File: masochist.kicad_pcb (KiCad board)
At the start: 2 copper layers, 202.4 x 100.8 mm, 88 parts, among them J1 USB_C_Receptacle_USB2.0, J2 AVR-ISP-6, SW1 RESET, SW2 SW_Push, U1 ATmega328P-PU, Y1 Crystal

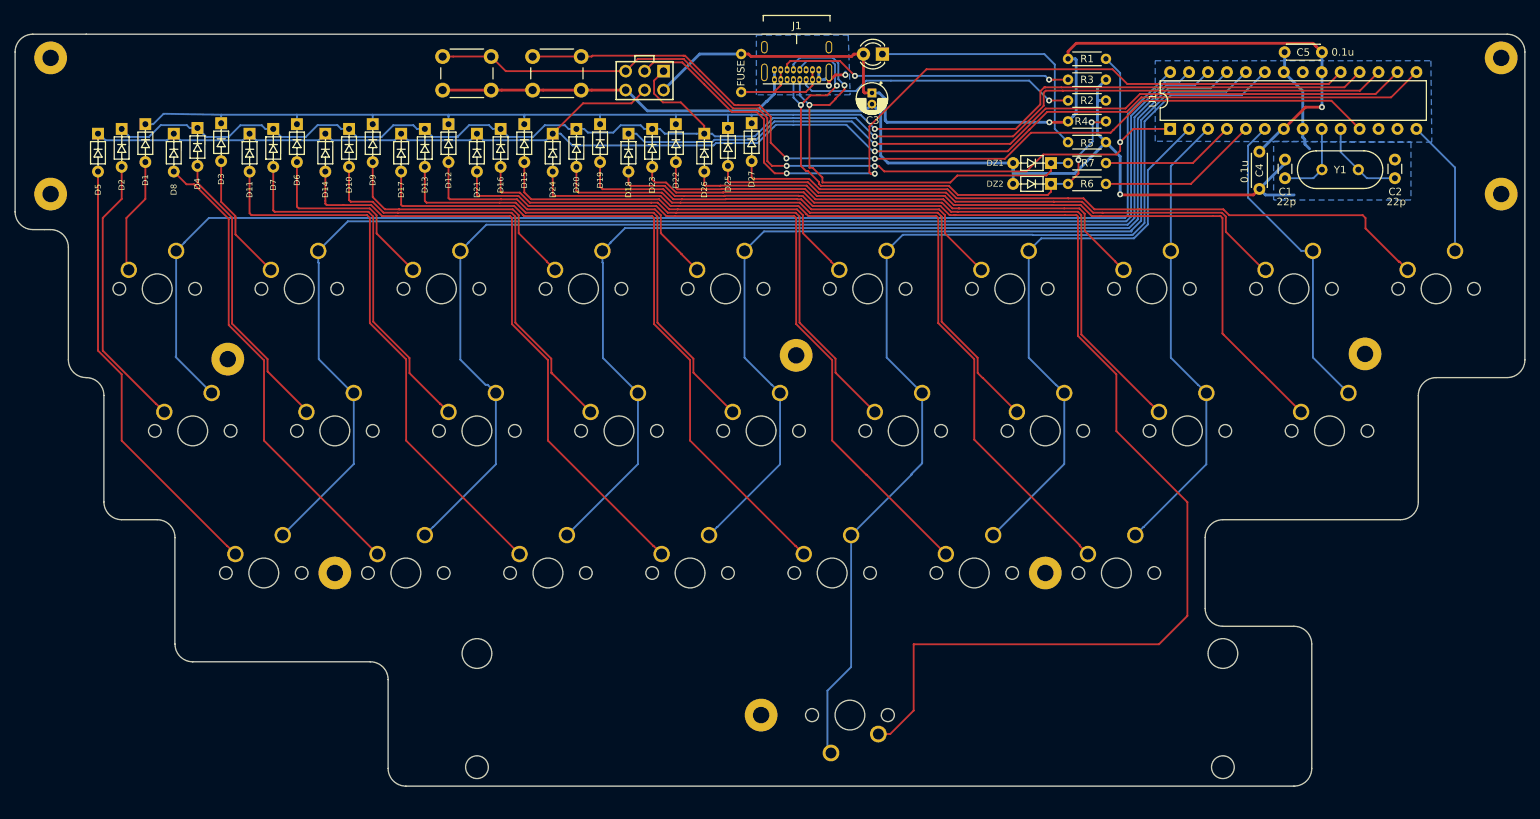
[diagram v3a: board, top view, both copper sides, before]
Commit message: added more mounting holes i love mounting holes
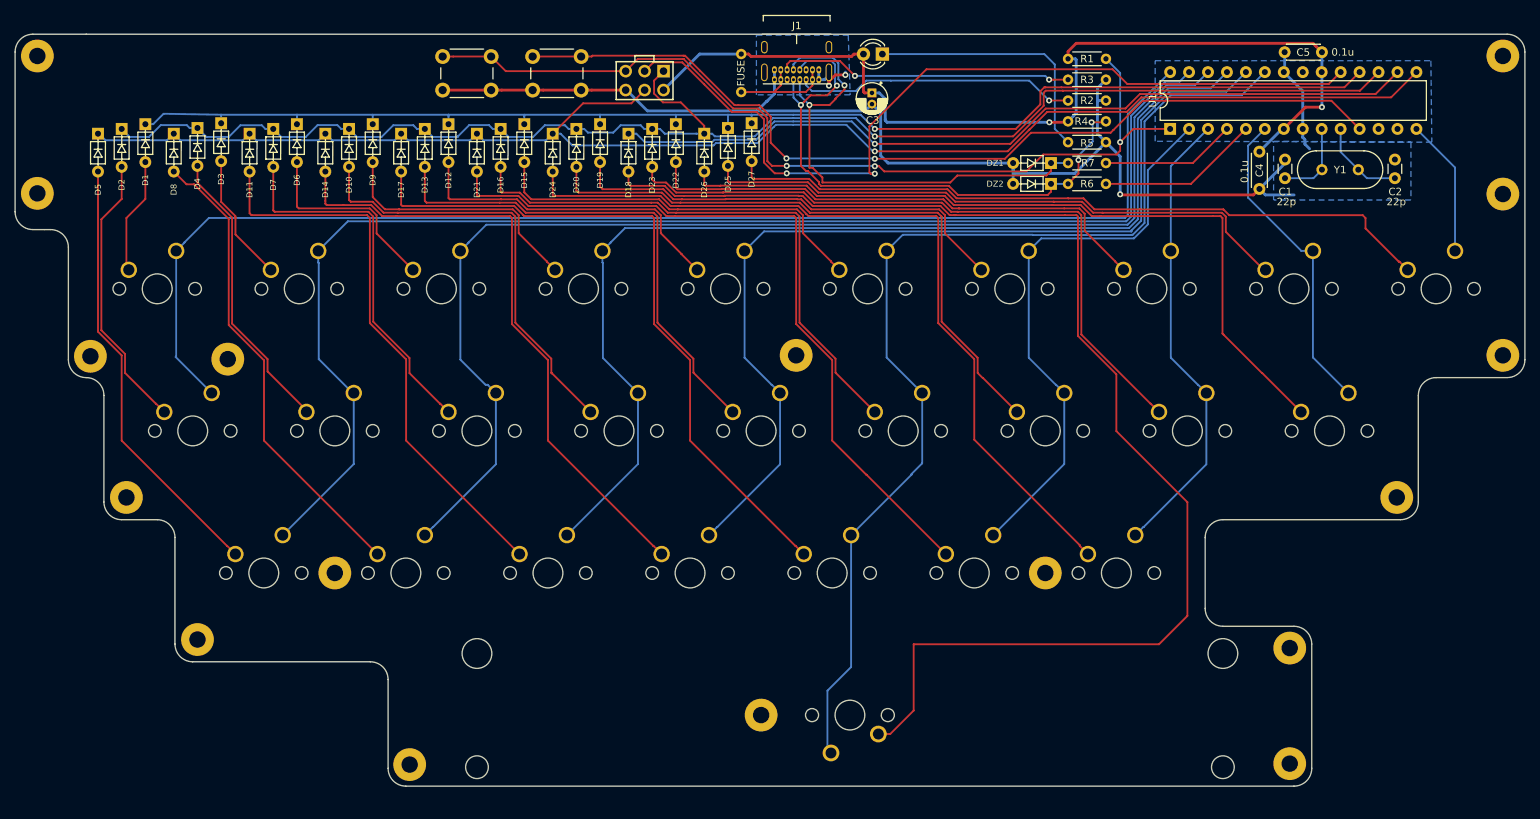
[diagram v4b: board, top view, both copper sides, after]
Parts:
- removed the REF** at (63.5, 34.9)
- removed the REF** at (258.0, 53.2)
- added REF**: MountingHole_2.2mm_M2_Pad, cftkb:MountingHole_2.2mm_M2_Pad, F.Cu at (68.8, 74.9)
- added REF**: MountingHole_2.2mm_M2_Pad, cftkb:MountingHole_2.2mm_M2_Pad, F.Cu at (61.7, 34.7)
- added REF**: MountingHole_2.2mm_M2_Pad, cftkb:MountingHole_2.2mm_M2_Pad, F.Cu at (258.2, 53.2)
- added REF**: MountingHole_2.2mm_M2_Pad, cftkb:MountingHole_2.2mm_M2_Pad, F.Cu at (73.7, 93.9)
- added REF**: MountingHole_2.2mm_M2_Pad, cftkb:MountingHole_2.2mm_M2_Pad, F.Cu at (83.2, 112.9)
- added REF**: MountingHole_2.2mm_M2_Pad, cftkb:MountingHole_2.2mm_M2_Pad, F.Cu at (111.6, 129.7)
- added REF**: MountingHole_2.2mm_M2_Pad, cftkb:MountingHole_2.2mm_M2_Pad, F.Cu at (229.6, 129.5)
- added REF**: MountingHole_2.2mm_M2_Pad, cftkb:MountingHole_2.2mm_M2_Pad, F.Cu at (229.6, 114.0)
- added REF**: MountingHole_2.2mm_M2_Pad, cftkb:MountingHole_2.2mm_M2_Pad, F.Cu at (244.0, 93.9)
- moved REF** 18.5 mm to (258.2, 74.8)
- moved G*** 4.83 mm to (163.4, 45.8)
- moved REF** 1.78 mm to (61.7, 53.1)
- moved REF** 0.34 mm to (258.2, 34.7)
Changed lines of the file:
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@@
     (thickness 1.6)
     (drawings 38)
-    (tracks 968)
+    (tracks 970)
     (zones 0)
-    (modules 88)
+    (modules 95)
     (nets 62)
   )
@@
     (add_net GND)
   )
+  (module cftkb:MountingHole_2.2mm_M2_Pad (layer F.Cu)
+    (at 68.834 74.93)
+    (descr "Mounting Hole 2.2mm, M2")
+    (tags "mounting hole 2.2mm m2")
+    (attr virtual)
+    (fp_text reference REF** (at 0 -3.2) (layer Cmts.User)
+      (effects (font (size 1 1) (thickness 0.15)))
+    )
+    (fp_text value MountingHole_2.2mm_M2_Pad (at 0 3.2) (layer F.Fab)
+      (effects (font (size 1 1) (thickness 0.15)))
+    )
+    (fp_circle (center 0 0) (end 2.45 0) (layer F.CrtYd) (width 0.05))
+    (fp_circle (center 0 0) (end 2.2 0) (layer Cmts.User) (width 0.15))
+    (fp_text user %R (at 0.3 0) (layer F.Fab)
+      (effects (font (size 1 1) (thickness 0.15)))
+    )
+    (pad 1 thru_hole circle (at 0 0) (size 4.4 4.4) (drill 2.2) (layers *.Cu *.Mask))
+  )
+  (module cftkb:MountingHole_2.2mm_M2_Pad (layer F.Cu)
+    (at 73.66 93.853)
+    (descr "Mounting Hole 2.2mm, M2")
+    (tags "mounting hole 2.2mm m2")
+    (attr virtual)
+    (fp_text reference REF** (at 0 -3.2) (layer Cmts.User)
+      (effects (font (size 1 1) (thickness 0.15)))
+    )
+    (fp_text value MountingHole_2.2mm_M2_Pad (at 0 3.2) (layer F.Fab)
+      (effects (font (size 1 1) (thickness 0.15)))
+    )
+    (fp_circle (center 0 0) (end 2.45 0) (layer F.CrtYd) (width 0.05))
+    (fp_circle (center 0 0) (end 2.2 0) (layer Cmts.User) (width 0.15))
+    (fp_text user %R (at 0.3 0) (layer F.Fab)
+      (effects (font (size 1 1) (thickness 0.15)))
+    )
+    (pad 1 thru_hole circle (at 0 0) (size 4.4 4.4) (drill 2.2) (layers *.Cu *.Mask))
+  )
+  (module cftkb:MountingHole_2.2mm_M2_Pad (layer F.Cu)
+    (at 83.185 112.903)
+    (descr "Mounting Hole 2.2mm, M2")
+    (tags "mounting hole 2.2mm m2")
+    (attr virtual)
+    (fp_text reference REF** (at 0 -3.2) (layer Cmts.User)
+      (effects (font (size 1 1) (thickness 0.15)))
+    )
+    (fp_text value MountingHole_2.2mm_M2_Pad (at 0 3.2) (layer F.Fab)
+      (effects (font (size 1 1) (thickness 0.15)))
+    )
+    (fp_circle (center 0 0) (end 2.45 0) (layer F.CrtYd) (width 0.05))
+    (fp_circle (center 0 0) (end 2.2 0) (layer Cmts.User) (width 0.15))
+    (fp_text user %R (at 0.3 0) (layer F.Fab)
+      (effects (font (size 1 1) (thickness 0.15)))
+    )
+    (pad 1 thru_hole circle (at 0 0) (size 4.4 4.4) (drill 2.2) (layers *.Cu *.Mask))
+  )
+  (module cftkb:MountingHole_2.2mm_M2_Pad (layer F.Cu)
+    (at 111.633 129.667)
+    (descr "Mounting Hole 2.2mm, M2")
+    (tags "mounting hole 2.2mm m2")
+    (attr virtual)
+    (fp_text reference REF** (at 0 -3.2) (layer Cmts.User)
+      (effects (font (size 1 1) (thickness 0.15)))
+    )
+    (fp_text value MountingHole_2.2mm_M2_Pad (at 0 3.2) (layer F.Fab)
+      (effects (font (size 1 1) (thickness 0.15)))
+    )
+    (fp_circle (center 0 0) (end 2.45 0) (layer F.CrtYd) (width 0.05))
+    (fp_circle (center 0 0) (end 2.2 0) (layer Cmts.User) (width 0.15))
+    (fp_text user %R (at 0.3 0) (layer F.Fab)
+      (effects (font (size 1 1) (thickness 0.15)))
+    )
+    (pad 1 thru_hole circle (at 0 0) (size 4.4 4.4) (drill 2.2) (layers *.Cu *.Mask))
+  )
+  (module cftkb:MountingHole_2.2mm_M2_Pad (layer F.Cu)
+    (at 229.616 129.54)
+    (descr "Mounting Hole 2.2mm, M2")
+    (tags "mounting hole 2.2mm m2")
+    (attr virtual)
+    (fp_text reference REF** (at 0 -3.2) (layer Cmts.User)
+      (effects (font (size 1 1) (thickness 0.15)))
+    )
+    (fp_text value MountingHole_2.2mm_M2_Pad (at 0 3.2) (layer F.Fab)
+      (effects (font (size 1 1) (thickness 0.15)))
+    )
+    (fp_circle (center 0 0) (end 2.45 0) (layer F.CrtYd) (width 0.05))
+    (fp_circle (center 0 0) (end 2.2 0) (layer Cmts.User) (width 0.15))
+    (fp_text user %R (at 0.3 0) (layer F.Fab)
+      (effects (font (size 1 1) (thickness 0.15)))
+    )
+    (pad 1 thru_hole circle (at 0 0) (size 4.4 4.4) (drill 2.2) (layers *.Cu *.Mask))
+  )
+  (module cftkb:MountingHole_2.2mm_M2_Pad (layer F.Cu)
+    (at 229.616 114.046)
+    (descr "Mounting Hole 2.2mm, M2")
+    (tags "mounting hole 2.2mm m2")
+    (attr virtual)
+    (fp_text reference REF** (at 0 -3.2) (layer Cmts.User)
+      (effects (font (size 1 1) (thickness 0.15)))
+    )
+    (fp_text value MountingHole_2.2mm_M2_Pad (at 0 3.2) (layer F.Fab)
+      (effects (font (size 1 1) (thickness 0.15)))
+    )
+    (fp_circle (center 0 0) (end 2.45 0) (layer F.CrtYd) (width 0.05))
+    (fp_circle (center 0 0) (end 2.2 0) (layer Cmts.User) (width 0.15))
+    (fp_text user %R (at 0.3 0) (layer F.Fab)
+      (effects (font (size 1 1) (thickness 0.15)))
+    )
+    (pad 1 thru_hole circle (at 0 0) (size 4.4 4.4) (drill 2.2) (layers *.Cu *.Mask))
+  )
+  (module cftkb:MountingHole_2.2mm_M2_Pad (layer F.Cu)
+    (at 243.967 93.853)
+    (descr "Mounting Hole 2.2mm, M2")
+    (tags "mounting hole 2.2mm m2")
+    (attr virtual)
+    (fp_text reference REF** (at 0 -3.2) (layer Cmts.User)
+      (effects (font (size 1 1) (thickness 0.15)))
+    )
+    (fp_text value MountingHole_2.2mm_M2_Pad (at 0 3.2) (layer F.Fab)
+      (effects (font (size 1 1) (thickness 0.15)))
+    )
+    (fp_circle (center 0 0) (end 2.45 0) (layer F.CrtYd) (width 0.05))
+    (fp_circle (center 0 0) (end 2.2 0) (layer Cmts.User) (width 0.15))
+    (fp_text user %R (at 0.3 0) (layer F.Fab)
+      (effects (font (size 1 1) (thickness 0.15)))
+    )
+    (pad 1 thru_hole circle (at 0 0) (size 4.4 4.4) (drill 2.2) (layers *.Cu *.Mask))
+  )
   (module silkscreen:reid_face_tiny (layer B.Cu)
-    (at 168.275 46.0375 180)
+    (at 163.449 45.847 180)
     (fp_text reference G*** (at 0 3.81) (layer B.SilkS) hide
       (effects (font (size 1.524 1.524) (thickness 0.3)) (justify mirror))
@@
   )
   (module cftkb:MountingHole_2.2mm_M2_Pad (layer F.Cu)
-    (at 63.5 53.18125)
+    (at 61.722 53.086)
     (descr "Mounting Hole 2.2mm, M2")
     (tags "mounting hole 2.2mm m2")
@@
   )
   (module cftkb:MountingHole_2.2mm_M2_Pad (layer F.Cu)
-    (at 63.5 34.925)
+    (at 61.722 34.671)
     (descr "Mounting Hole 2.2mm, M2")
     (tags "mounting hole 2.2mm m2")
@@
   )
   (module cftkb:MountingHole_2.2mm_M2_Pad (layer F.Cu)
-    (at 257.96875 53.18125)
+    (at 258.191 53.18125)
     (descr "Mounting Hole 2.2mm, M2")
     (tags "mounting hole 2.2mm m2")
@@
   )
   (module cftkb:MountingHole_2.2mm_M2_Pad (layer F.Cu)
-    (at 257.96875 34.925)
+    (at 258.191 34.671)
     (descr "Mounting Hole 2.2mm, M2")
     (tags "mounting hole 2.2mm m2")
@@
   )
   (module cftkb:MountingHole_2.2mm_M2_Pad (layer F.Cu)
-    (at 239.7125 74.6125)
+    (at 258.191 74.803)
     (descr "Mounting Hole 2.2mm, M2")
     (tags "mounting hole 2.2mm m2")
@@
   (segment (start 77.640001 81.291251) (end 77.608251 81.291251) (width 0.25) (layer F.Cu) (net 7))
   (segment (start 78.74 82.39125) (end 77.640001 81.291251) (width 0.25) (layer F.Cu) (net 7))
-  (segment (start 70.485 74.168) (end 70.485 56.388) (width 0.25) (layer F.Cu) (net 7))
-  (segment (start 77.608251 81.291251) (end 70.485 74.168) (width 0.25) (layer F.Cu) (net 7))
-  (segment (start 70.485 56.388) (end 73.025 53.848) (width 0.25) (layer F.Cu) (net 7))
+  (segment (start 73.47501 77.15801) (end 73.475009 74.616599) (width 0.25) (layer F.Cu) (net 7))
+  (segment (start 77.608251 81.291251) (end 73.47501 77.15801) (width 0.25) (layer F.Cu) (net 7))
+  (segment (start 73.475009 74.616599) (end 70.30001 71.4416) (width 0.25) (layer F.Cu) (net 7))
+  (segment (start 70.30001 56.57299) (end 73.025 53.848) (width 0.25) (layer F.Cu) (net 7))
+  (segment (start 70.30001 71.4416) (end 70.30001 56.57299) (width 0.25) (layer F.Cu) (net 7))
   (segment (start 73.025 44.45) (end 73.787 45.212) (width 0.25) (layer B.Cu) (net 8))
   (segment (start 73.787 45.212) (end 74.09899 45.52399) (width 0.25) (layer B.Cu) (net 8))
@@
   (segment (start 87.82601 70.5526) (end 87.826009 56.328599) (width 0.25) (layer F.Cu) (net 10))
   (segment (start 83.185 51.68759) (end 83.185 49.403) (width 0.25) (layer F.Cu) (net 10))
-  (segment (start 69.85 74.16941) (end 69.85 50.165) (width 0.25) (layer F.Cu) (net 11))
-  (segment (start 87.133251 100.341251) (end 73.025 86.233) (width 0.25) (layer F.Cu) (net 11))
+  (segment (start 69.85 71.628) (end 69.85 50.165) (width 0.25) (layer F.Cu) (net 11))
   (segment (start 88.265 101.44125) (end 87.165001 100.341251) (width 0.25) (layer F.Cu) (net 11))
-  (segment (start 73.025 77.34441) (end 69.85 74.16941) (width 0.25) (layer F.Cu) (net 11))
+  (segment (start 87.133251 100.341251) (end 73.025 86.233) (width 0.25) (layer F.Cu) (net 11))
+  (segment (start 73.025 74.803) (end 69.85 71.628) (width 0.25) (layer F.Cu) (net 11))
   (segment (start 87.165001 100.341251) (end 87.133251 100.341251) (width 0.25) (layer F.Cu) (net 11))
-  (segment (start 73.025 86.233) (end 73.025 77.34441) (width 0.25) (layer F.Cu) (net 11))
+  (segment (start 73.025 86.233) (end 73.025 74.803) (width 0.25) (layer F.Cu) (net 11))
   (segment (start 70.866 45.974) (end 79.121 45.974) (width 0.25) (layer B.Cu) (net 12))
   (segment (start 79.121 45.974) (end 80.01 45.085) (width 0.25) (layer B.Cu) (net 12))
